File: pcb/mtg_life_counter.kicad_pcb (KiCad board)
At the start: 2 copper layers, 167.6 x 101.6 mm, 89 parts, among them J1 USB C 4907, J2 ICSP, SW1 SW_SPST, SW2 SW_SPST, U1 ATmega328P-AU, U2 74HC595, U3 74HC595, U4 74HC595, U5 74HC595, U6 TPIC6B595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

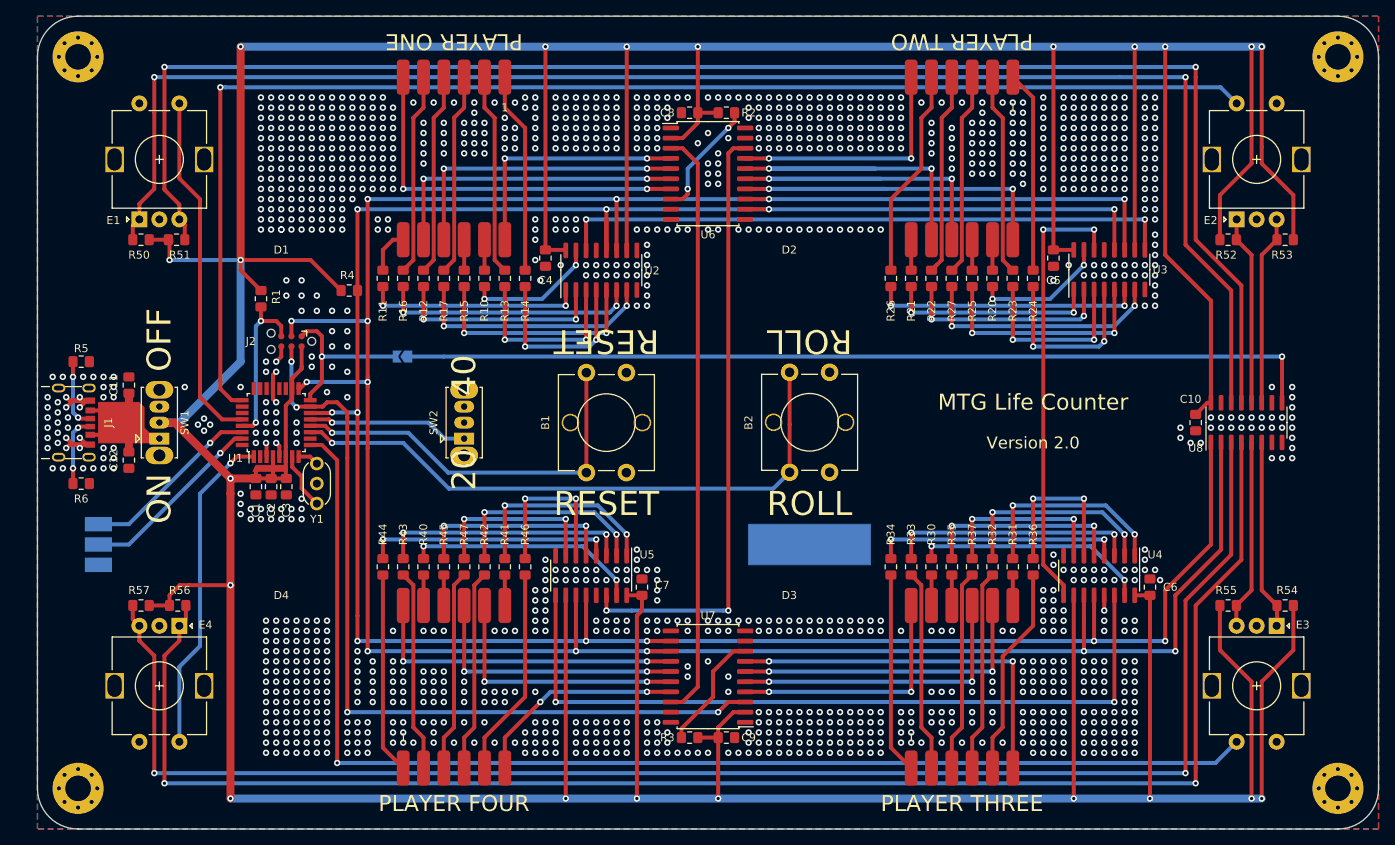
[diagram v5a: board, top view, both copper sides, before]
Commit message: Separate display and encoder latch lines
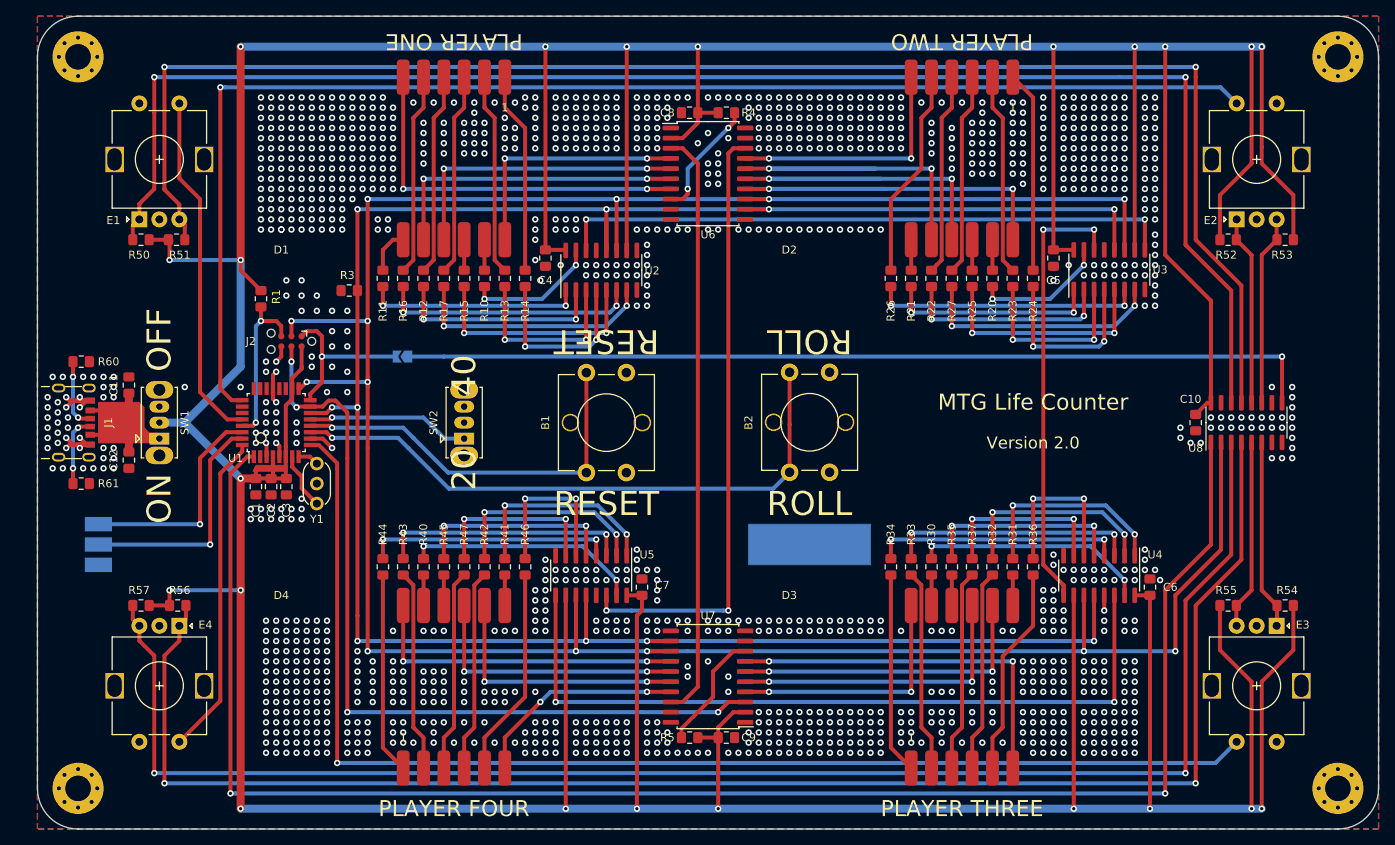
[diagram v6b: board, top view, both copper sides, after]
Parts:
- renumbered R4 to R3, R2 to R4, R3 to R5, R5 to R60, R6 to R61
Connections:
- R3 pad 1: +5V -> GND
- R3 pad 2: /SER_LATCH -> /DISP_LATCH
- U1 pad 1: /E4_SW -> /ENC_LATCH
- U1 pad 14: /SER_LATCH -> /DISP_LATCH
- U1 pad 32: Net-(U1-Pad32) -> /E4_SW
- U2 pad 12: /SER_LATCH -> /DISP_LATCH
- U3 pad 12: /SER_LATCH -> /DISP_LATCH
- U4 pad 12: /SER_LATCH -> /DISP_LATCH
- U5 pad 12: /SER_LATCH -> /DISP_LATCH
- U6 pad 12: /SER_LATCH -> /DISP_LATCH
- U7 pad 12: /SER_LATCH -> /DISP_LATCH
- U8 pad 1: /SER_LATCH -> /ENC_LATCH
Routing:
- net /SER_LATCH: track 314.2 -> 0.00 mm, vias 11 -> 0
- net /DISP_LATCH: track 0.00 -> 278.3 mm, vias 0 -> 10
- net /ENC_LATCH: track 0.00 -> 206.9 mm, vias 0 -> 2
- net +5V: track 918.9 -> 912.2 mm, vias 21 -> 22
- net /D1(TX): track 23.5 -> 29.6 mm
- net /D0(RX): track 22.7 -> 27.6 mm
- net Net-(U1-Pad10): track 0.00 -> 3.22 mm, vias 0 -> 1
- net Net-(U1-Pad32): track 0.52 -> 0.00 mm
- net /E4_SW: track 40.7 -> 40.9 mm, vias 1 -> 0
- net GND: vias 1328 -> 1321
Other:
- board text added: "TODO - Verify encoder footprint (mounting points) - Add pullup on ENC_LATCH"
- board text removed: "TODO - Verify encoder footprint (mounting points)"

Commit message: Add protection diode. Finalize test points + jumpers
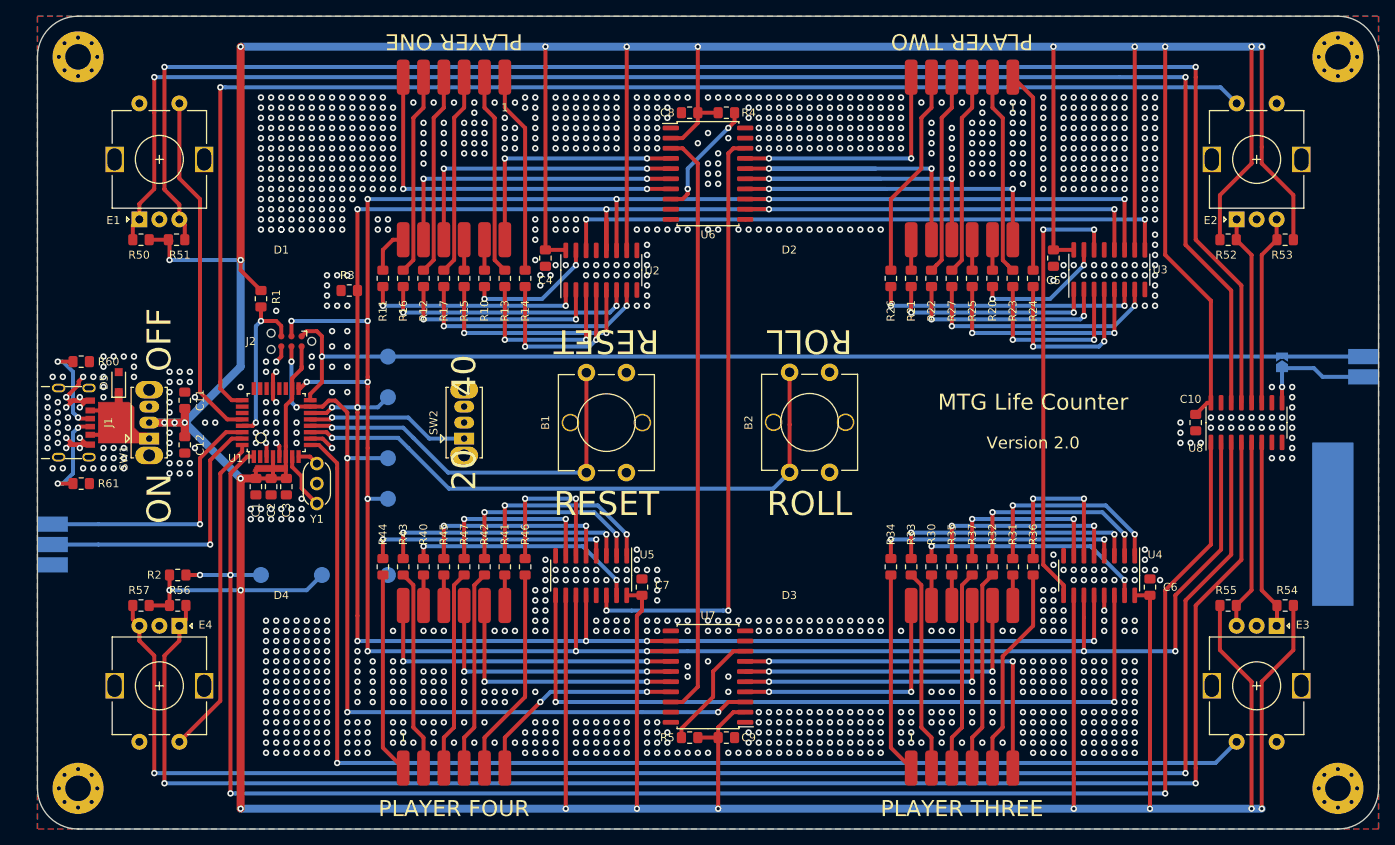
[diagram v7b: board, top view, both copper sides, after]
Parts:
- added D5: PJSD05W_R1_00001, Diode_SMD:D_SOD-323_HandSoldering, F.Cu at (61.0, 96.5)
- added J3: TP_UART, mtg_life_counter:TP_Edge_3, B.Cu at (54.6, 114.3)
- added JP2: JP_SR, mtg_life_counter:TP_Edge_2, B.Cu at (218.4, 93.3)
- added R2: 10k, Resistor_SMD:R_0805_2012Metric_Pad1.15x1.40mm_HandSolder, F.Cu at (68.3, 120.7)
- added TP4: SCLK, TestPoint:TestPoint_Pad_D2.0mm, B.Cu at (94.6, 111.1)
- added TP5: E_LAT, TestPoint:TestPoint_Pad_D2.0mm, B.Cu at (78.7, 120.7)
- added TP6: GND, TestPoint:TestPoint_Pad_D2.0mm, B.Cu at (94.6, 120.7)
- added TP7: 5V, TestPoint:TestPoint_Pad_D2.0mm, B.Cu at (86.4, 120.7)
- C12: value 1uF -> 10uF
- TP1: value TX -> CIPO; footprint TestPoint:TestPoint_Keystone_5015_Micro-Minature -> TestPoint:TestPoint_Pad_D2.0mm
- TP2: value RX -> D_LAT; footprint TestPoint:TestPoint_Keystone_5015_Micro-Minature -> TestPoint:TestPoint_Pad_D2.0mm
- TP3: value GND -> COPI; footprint TestPoint:TestPoint_Keystone_5015_Micro-Minature -> TestPoint:TestPoint_Pad_D2.0mm
- moved JP1 109.9 mm to (206.4, 94.1), turned to 90 degrees
- moved TP1 43.2 mm to (94.6, 93.3)
- moved TP2 39.5 mm to (94.6, 98.4)
- moved TP3 38.6 mm to (94.6, 106.0)
- moved C11 7.24 mm to (69.2, 98.8)
- moved C12 7.24 mm to (69.2, 104.4)
- moved SW1 1.27 mm to (64.8, 103.6)
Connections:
- C11 pad 2: VBUS -> +5V
- C12 pad 2: VBUS -> +5V
- J2 pad 1: /SER_MISO -> /SER_CIPO
- J2 pad 4: /SER_MOSI -> /SER_COPI
- JP1 pad 2: /SER_MISO -> /SER_CIPO
- TP1 pad 1: /D1(TX) -> /SER_CIPO
- TP2 pad 1: /D0(RX) -> /DISP_LATCH
- TP3 pad 1: GND -> /SER_COPI
- U1 pad 15: /SER_MOSI -> /SER_COPI
- U1 pad 16: /SER_MISO -> /SER_CIPO
- U7 pad 3: /SER_MOSI -> /SER_COPI
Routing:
- net /SER_CIPO: track 0.00 -> 142.4 mm, vias 0 -> 1
- net /SER_COPI: track 0.00 -> 108.0 mm, vias 0 -> 5
- net /SER_MOSI: track 102.9 -> 0.00 mm, vias 4 -> 0
- net /SR_OUT: track 115.0 -> 14.9 mm
- net +5V: track 912.2 -> 934.3 mm, vias 22 -> 25
- net /SER_MISO: track 21.5 -> 0.00 mm, vias 1 -> 0
- net /ENC_LATCH: track 206.9 -> 216.3 mm, vias 2 -> 4
- net VBUS: track 25.3 -> 16.5 mm
- net /D1(TX): track 29.6 -> 35.3 mm
- net /D0(RX): track 27.6 -> 33.3 mm
- net /DISP_LATCH: track 278.3 -> 282.7 mm
- net GND: track 31.2 -> 34.6 mm, vias 1321 -> 1355
- net Net-(J1-PadB5): track 8.82 -> 11.9 mm
- net Net-(J1-PadA5): track 8.82 -> 11.9 mm
- net /SER_CLK: track 334.1 -> 336.6 mm, vias 13 -> 14
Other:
- board text added: "GND"
- board text added: "RX"
- board text added: "SERIAL"
- board text added: "TX"
- board text removed: "Serial"
- board text removed: "TODO - Verify encoder footprint (mounting points) - Add pullup on ENC_LATCH"

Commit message: Resolve design review issues
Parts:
- added R6: 10k, Resistor_SMD:R_0805_2012Metric_Pad1.15x1.40mm_HandSolder, B.Cu at (210.2, 94.4)
- moved TP6 24.8 mm to (110.5, 101.6)
- moved C4 0.64 mm to (114.9, 81.0)
- moved C5 0.63 mm to (178.4, 81.0)
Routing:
- net GND: track 34.6 -> 179.8 mm, vias 1355 -> 494
- net +5V: track 934.3 -> 933.0 mm
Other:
- board text removed: "+5 polygon pour under U8 and arduino and caps"
- board text removed: "1uF cap by the USB, after the switch"
- board text removed: "Add teardropping on through hole pads"
- board text removed: "Adjust traces by resonator to get copper pour up to pin 9 on uC"
- board text removed: "Check for USB termination resistor requirements"
- board text removed: "ESD protection diodes Clamping zener 20V+ varistor"
- board text removed: "GROUND STICTICHIN!!!"
- board text removed: "Increase power trace width"
- board text removed: "Look for dangly bits on the pours"
- board text removed: "add some DNP caps + resistors on clk and latch lines connect them roughly in order of the serial link close the C"
- board text removed: "bigger exposed copper on ground lugs"
- board text removed: "double up traces under usb"
